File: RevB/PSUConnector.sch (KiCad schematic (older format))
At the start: 14 parts

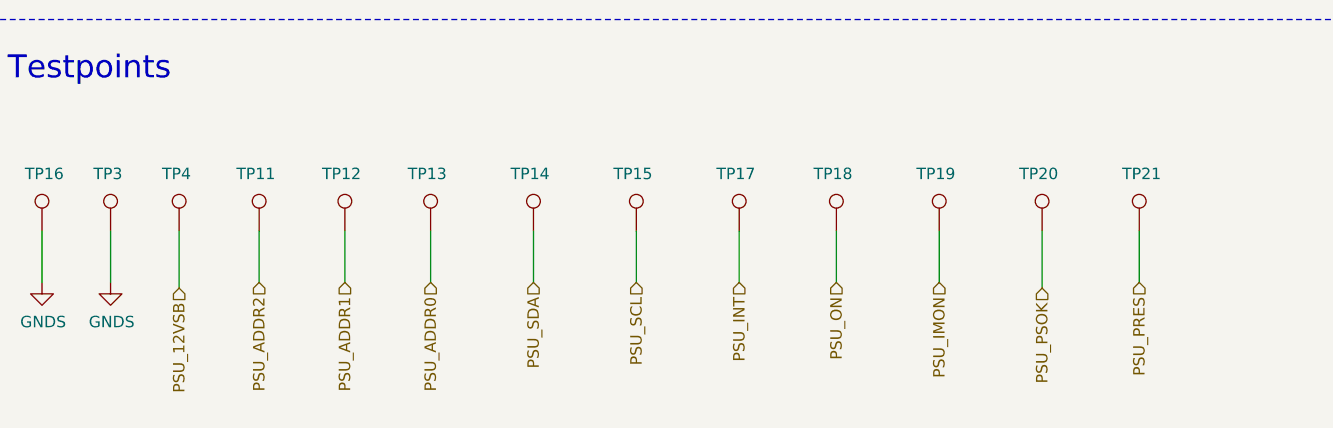
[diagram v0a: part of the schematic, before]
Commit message: hw update
- changed third dip switch to cd4066 and spdt slide switch
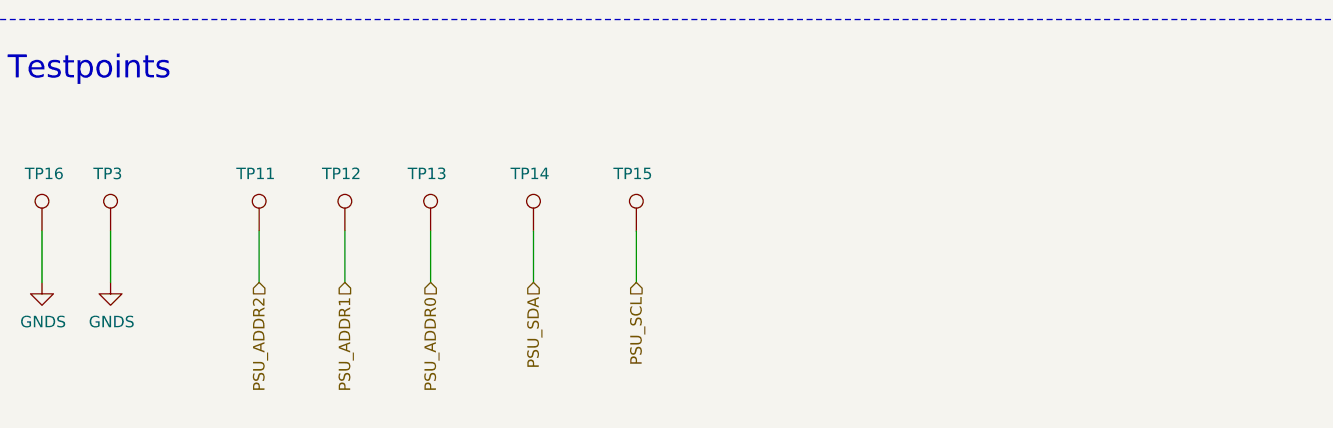
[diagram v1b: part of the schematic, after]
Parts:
- removed TP17, TP18, TP19, TP20, TP21, TP4: TestPoint, TestPoint:TestPoint_Pad_1.0x1.0mm, symbol Connector:TestPoint
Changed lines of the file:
@@
 Text HLabel 4750 4075 0    50   Input ~ 0
 PSU_ADDR2
+Text Notes 1225 1250 0    100  ~ 0
+Card Slot Connector
+Text Notes 1100 6075 0    100  ~ 0
+Testpoints
+Wire Notes Line
+	1025 5800 10425 5800
 $Comp
-L Connector:TestPoint TP?
-U 1 1 5F18B86B
-P 1550 6725
-AR Path="/5F02F4E9/5F18B86B" Ref="TP?"  Part="1"
-AR Path="/5EFF0F4B/5F18B86B" Ref="TP3"  Part="1"
-F 0 "TP3" H 1475 6975 50  0000 L CNN
-F 1 "TestPoint" H 1400 7000 50  0001 L CNN
-F 2 "TestPoint:TestPoint_Pad_1.0x1.0mm" H 1750 6725 50  0001 C CNN
-F 3 "~" H 1750 6725 50  0001 C CNN
-	1    1550 6725
-	1    0    0    -1
-$EndComp
-$Comp
-L Connector:TestPoint TP?
-U 1 1 5F18F46B
-P 1850 6725
-AR Path="/5F02F4E9/5F18F46B" Ref="TP?"  Part="1"
-AR Path="/5EFF0F4B/5F18F46B" Ref="TP4"  Part="1"
-F 0 "TP4" H 1775 6975 50  0000 L CNN
-F 1 "TestPoint" H 1908 6752 50  0001 L CNN
-F 2 "TestPoint:TestPoint_Pad_1.0x1.0mm" H 2050 6725 50  0001 C CNN
-F 3 "~" H 2050 6725 50  0001 C CNN
-	1    1850 6725
+L power:GNDS #PWR016
+U 1 1 5F20C83E
+P 1250 6950
+F 0 "#PWR016" H 1250 6700 50  0001 C CNN
+F 1 "GNDS" H 1255 6777 50  0000 C CNN
+F 2 "" H 1250 6950 50  0001 C CNN
+F 3 "" H 1250 6950 50  0001 C CNN
+	1    1250 6950
 	1    0    0    -1
 $EndComp
 Wire Wire Line
-	1550 6725 1550 6950
+	1250 6725 1250 6950
 $Comp
-L power:GNDS #PWR015
-U 1 1 5F196630
-P 1550 6950
-F 0 "#PWR015" H 1550 6700 50  0001 C CNN
-F 1 "GNDS" H 1555 6777 50  0000 C CNN
-F 2 "" H 1550 6950 50  0001 C CNN
-F 3 "" H 1550 6950 50  0001 C CNN
-	1    1550 6950
+L Connector:TestPoint TP?
+U 1 1 5F208833
+P 1250 6725
+AR Path="/5F02F4E9/5F208833" Ref="TP?"  Part="1"
+AR Path="/5EFF0F4B/5F208833" Ref="TP16"  Part="1"
+F 0 "TP16" H 1175 6975 50  0000 L CNN
+F 1 "TestPoint" H 1308 6752 50  0001 L CNN
+F 2 "TestPoint:TestPoint_Pad_1.0x1.0mm" H 1450 6725 50  0001 C CNN
+F 3 "~" H 1450 6725 50  0001 C CNN
+	1    1250 6725
+	1    0    0    -1
+$EndComp
+Text HLabel 3850 6950 3    50   Input ~ 0
+PSU_SCL
+Text HLabel 3400 6950 3    50   Input ~ 0
+PSU_SDA
+Wire Wire Line
+	3400 6725 3400 6950
+$Comp
+L Connector:TestPoint TP?
+U 1 1 5F1FA086
+P 3400 6725
+AR Path="/5F02F4E9/5F1FA086" Ref="TP?"  Part="1"
+AR Path="/5EFF0F4B/5F1FA086" Ref="TP14"  Part="1"
+F 0 "TP14" H 3300 6975 50  0000 L CNN
+F 1 "TestPoint" H 3458 6752 50  0001 L CNN
+F 2 "TestPoint:TestPoint_Pad_1.0x1.0mm" H 3600 6725 50  0001 C CNN
+F 3 "~" H 3600 6725 50  0001 C CNN
+	1    3400 6725
 	1    0    0    -1
 $EndComp
 Wire Wire Line
-	1850 6725 1850 6975
-Text HLabel 1850 6975 3    50   Input ~ 0
-PSU_12VSB
+	3850 6725 3850 6950
 $Comp
 L Connector:TestPoint TP?
-U 1 1 5F1D2F4B
-P 2575 6725
-AR Path="/5F02F4E9/5F1D2F4B" Ref="TP?"  Part="1"
-AR Path="/5EFF0F4B/5F1D2F4B" Ref="TP12"  Part="1"
-F 0 "TP12" H 2475 6975 50  0000 L CNN
-F 1 "TestPoint" H 2633 6752 50  0001 L CNN
-F 2 "TestPoint:TestPoint_Pad_1.0x1.0mm" H 2775 6725 50  0001 C CNN
-F 3 "~" H 2775 6725 50  0001 C CNN
-	1    2575 6725
+U 1 1 5F1FA07F
+P 3850 6725
+AR Path="/5F02F4E9/5F1FA07F" Ref="TP?"  Part="1"
+AR Path="/5EFF0F4B/5F1FA07F" Ref="TP15"  Part="1"
+F 0 "TP15" H 3750 6975 50  0000 L CNN
+F 1 "TestPoint" H 3908 6752 50  0001 L CNN
+F 2 "TestPoint:TestPoint_Pad_1.0x1.0mm" H 4050 6725 50  0001 C CNN
+F 3 "~" H 4050 6725 50  0001 C CNN
+	1    3850 6725
+	1    0    0    -1
+$EndComp
+Text HLabel 2200 6950 3    50   Input ~ 0
+PSU_ADDR2
+Text HLabel 2575 6950 3    50   Input ~ 0
+PSU_ADDR1
+Text HLabel 2950 6950 3    50   Input ~ 0
+PSU_ADDR0
+Wire Wire Line
+	2200 6725 2200 6950
+$Comp
+L Connector:TestPoint TP?
+U 1 1 5F1DA7F0
+P 2200 6725
+AR Path="/5F02F4E9/5F1DA7F0" Ref="TP?"  Part="1"
+AR Path="/5EFF0F4B/5F1DA7F0" Ref="TP11"  Part="1"
+F 0 "TP11" H 2100 6975 50  0000 L CNN
+F 1 "TestPoint" H 2258 6752 50  0001 L CNN
+F 2 "TestPoint:TestPoint_Pad_1.0x1.0mm" H 2400 6725 50  0001 C CNN
+F 3 "~" H 2400 6725 50  0001 C CNN
+	1    2200 6725
 	1    0    0    -1
 $EndComp
 Wire Wire Line
-	2575 6725 2575 6950
+	2950 6725 2950 6950
 $Comp
 L Connector:TestPoint TP?
@@
 $EndComp
 Wire Wire Line
-	2950 6725 2950 6950
+	2575 6725 2575 6950
 $Comp
 L Connector:TestPoint TP?
-U 1 1 5F1DA7F0
-P 2200 6725
-AR Path="/5F02F4E9/5F1DA7F0" Ref="TP?"  Part="1"
-AR Path="/5EFF0F4B/5F1DA7F0" Ref="TP11"  Part="1"
-F 0 "TP11" H 2100 6975 50  0000 L CNN
-F 1 "TestPoint" H 2258 6752 50  0001 L CNN
-F 2 "TestPoint:TestPoint_Pad_1.0x1.0mm" H 2400 6725 50  0001 C CNN
-F 3 "~" H 2400 6725 50  0001 C CNN
-	1    2200 6725
+U 1 1 5F1D2F4B
+P 2575 6725
+AR Path="/5F02F4E9/5F1D2F4B" Ref="TP?"  Part="1"
+AR Path="/5EFF0F4B/5F1D2F4B" Ref="TP12"  Part="1"
+F 0 "TP12" H 2475 6975 50  0000 L CNN
+F 1 "TestPoint" H 2633 6752 50  0001 L CNN
+F 2 "TestPoint:TestPoint_Pad_1.0x1.0mm" H 2775 6725 50  0001 C CNN
+F 3 "~" H 2775 6725 50  0001 C CNN
+	1    2575 6725
+	1    0    0    -1
+$EndComp
+$Comp
+L power:GNDS #PWR015
+U 1 1 5F196630
+P 1550 6950
+F 0 "#PWR015" H 1550 6700 50  0001 C CNN
+F 1 "GNDS" H 1555 6777 50  0000 C CNN
+F 2 "" H 1550 6950 50  0001 C CNN
+F 3 "" H 1550 6950 50  0001 C CNN
+	1    1550 6950
 	1    0    0    -1
 $EndComp
 Wire Wire Line
-	2200 6725 2200 6950
-Text HLabel 2950 6950 3    50   Input ~ 0
-PSU_ADDR0
-Text HLabel 2575 6950 3    50   Input ~ 0
-PSU_ADDR1
-Text HLabel 2200 6950 3    50   Input ~ 0
-PSU_ADDR2
+	1550 6725 1550 6950
 $Comp
 L Connector:TestPoint TP?
-U 1 1 5F1FA07F
-P 3850 6725
-AR Path="/5F02F4E9/5F1FA07F" Ref="TP?"  Part="1"
-AR Path="/5EFF0F4B/5F1FA07F" Ref="TP15"  Part="1"
-F 0 "TP15" H 3750 6975 50  0000 L CNN
-F 1 "TestPoint" H 3908 6752 50  0001 L CNN
-F 2 "TestPoint:TestPoint_Pad_1.0x1.0mm" H 4050 6725 50  0001 C CNN
-F 3 "~" H 4050 6725 50  0001 C CNN
-	1    3850 6725
+U 1 1 5F18B86B
+P 1550 6725
+AR Path="/5F02F4E9/5F18B86B" Ref="TP?"  Part="1"
+AR Path="/5EFF0F4B/5F18B86B" Ref="TP3"  Part="1"
+F 0 "TP3" H 1475 6975 50  0000 L CNN
+F 1 "TestPoint" H 1400 7000 50  0001 L CNN
+F 2 "TestPoint:TestPoint_Pad_1.0x1.0mm" H 1750 6725 50  0001 C CNN
+F 3 "~" H 1750 6725 50  0001 C CNN
+	1    1550 6725
 	1    0    0    -1
 $EndComp
-Wire Wire Line
-	3850 6725 3850 6950
-$Comp
-L Connector:TestPoint TP?
-U 1 1 5F1FA086
-P 3400 6725
-AR Path="/5F02F4E9/5F1FA086" Ref="TP?"  Part="1"
-AR Path="/5EFF0F4B/5F1FA086" Ref="TP14"  Part="1"
-F 0 "TP14" H 3300 6975 50  0000 L CNN
-F 1 "TestPoint" H 3458 6752 50  0001 L CNN
-F 2 "TestPoint:TestPoint_Pad_1.0x1.0mm" H 3600 6725 50  0001 C CNN
-F 3 "~" H 3600 6725 50  0001 C CNN
-	1    3400 6725
-	1    0    0    -1
-$EndComp
-Wire Wire Line
-	3400 6725 3400 6950
-Text HLabel 3400 6950 3    50   Input ~ 0
-PSU_SDA
-Text HLabel 3850 6950 3    50   Input ~ 0
-PSU_SCL
-$Comp
-L Connector:TestPoint TP?
-U 1 1 5F208833
-P 1250 6725
-AR Path="/5F02F4E9/5F208833" Ref="TP?"  Part="1"
-AR Path="/5EFF0F4B/5F208833" Ref="TP16"  Part="1"
-F 0 "TP16" H 1175 6975 50  0000 L CNN
-F 1 "TestPoint" H 1308 6752 50  0001 L CNN
-F 2 "TestPoint:TestPoint_Pad_1.0x1.0mm" H 1450 6725 50  0001 C CNN
-F 3 "~" H 1450 6725 50  0001 C CNN
-	1    1250 6725
-	1    0    0    -1
-$EndComp
-Wire Wire Line
-	1250 6725 1250 6950
-$Comp
-L power:GNDS #PWR016
-U 1 1 5F20C83E
-P 1250 6950
-F 0 "#PWR016" H 1250 6700 50  0001 C CNN
-F 1 "GNDS" H 1255 6777 50  0000 C CNN
-F 2 "" H 1250 6950 50  0001 C CNN
-F 3 "" H 1250 6950 50  0001 C CNN
-	1    1250 6950
-	1    0    0    -1
-$EndComp
-$Comp
-L Connector:TestPoint TP?
-U 1 1 5F221423
-P 4725 6725
-AR Path="/5F02F4E9/5F221423" Ref="TP?"  Part="1"
-AR Path="/5EFF0F4B/5F221423" Ref="TP18"  Part="1"
-F 0 "TP18" H 4625 6975 50  0000 L CNN
-F 1 "TestPoint" H 4783 6752 50  0001 L CNN
-F 2 "TestPoint:TestPoint_Pad_1.0x1.0mm" H 4925 6725 50  0001 C CNN
-F 3 "~" H 4925 6725 50  0001 C CNN
-	1    4725 6725
-	1    0    0    -1
-$EndComp
-Wire Wire Line
-	4725 6725 4725 6950
-$Comp
-L Connector:TestPoint TP?
-U 1 1 5F225748
-P 5175 6725
-AR Path="/5F02F4E9/5F225748" Ref="TP?"  Part="1"
-AR Path="/5EFF0F4B/5F225748" Ref="TP19"  Part="1"
-F 0 "TP19" H 5075 6975 50  0000 L CNN
-F 1 "TestPoint" H 5233 6752 50  0001 L CNN
-F 2 "TestPoint:TestPoint_Pad_1.0x1.0mm" H 5375 6725 50  0001 C CNN
-F 3 "~" H 5375 6725 50  0001 C CNN
-	1    5175 6725
-	1    0    0    -1
-$EndComp
-Wire Wire Line
-	5175 6725 5175 6950
-Text HLabel 5175 6950 3    50   Input ~ 0
-PSU_IMON
-Text HLabel 4725 6950 3    50   Input ~ 0
-PSU_ON
-$Comp
-L Connector:TestPoint TP?
-U 1 1 5F24027B
-P 5625 6725
-AR Path="/5F02F4E9/5F24027B" Ref="TP?"  Part="1"
-AR Path="/5EFF0F4B/5F24027B" Ref="TP20"  Part="1"
-F 0 "TP20" H 5525 6975 50  0000 L CNN
-F 1 "TestPoint" H 5683 6752 50  0001 L CNN
-F 2 "TestPoint:TestPoint_Pad_1.0x1.0mm" H 5825 6725 50  0001 C CNN
-F 3 "~" H 5825 6725 50  0001 C CNN
-	1    5625 6725
-	1    0    0    -1
-$EndComp
-Wire Wire Line
-	5625 6725 5625 6975
-Text HLabel 5625 6975 3    50   Input ~ 0
-PSU_PSOK
-$Comp
-L Connector:TestPoint TP?
-U 1 1 5F257476
-P 4300 6725
-AR Path="/5F02F4E9/5F257476" Ref="TP?"  Part="1"
-AR Path="/5EFF0F4B/5F257476" Ref="TP17"  Part="1"
-F 0 "TP17" H 4200 6975 50  0000 L CNN
-F 1 "TestPoint" H 4358 6752 50  0001 L CNN
-F 2 "TestPoint:TestPoint_Pad_1.0x1.0mm" H 4500 6725 50  0001 C CNN
-F 3 "~" H 4500 6725 50  0001 C CNN
-	1    4300 6725
-	1    0    0    -1
-$EndComp
-Wire Wire Line
-	4300 6725 4300 6950
-Text HLabel 4300 6950 3    50   Input ~ 0
-PSU_INT
-Text HLabel 6050 6950 3    50   Input ~ 0
-PSU_PRES
-$Comp
-L Connector:TestPoint TP?
-U 1 1 5F263862
-P 6050 6725
-AR Path="/5F02F4E9/5F263862" Ref="TP?"  Part="1"
-AR Path="/5EFF0F4B/5F263862" Ref="TP21"  Part="1"
-F 0 "TP21" H 5975 6975 50  0000 L CNN
-F 1 "TestPoint" H 6108 6752 50  0001 L CNN
-F 2 "TestPoint:TestPoint_Pad_1.0x1.0mm" H 6250 6725 50  0001 C CNN
-F 3 "~" H 6250 6725 50  0001 C CNN
-	1    6050 6725
-	1    0    0    -1
-$EndComp
-Wire Wire Line
-	6050 6725 6050 6950
-Wire Notes Line
-	1025 5800 10425 5800
-Text Notes 1100 6075 0    100  ~ 0
-Testpoints
-Text Notes 1225 1250 0    100  ~ 0
-Card Slot Connector
 $EndSCHEMATC
